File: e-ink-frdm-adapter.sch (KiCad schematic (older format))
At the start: 23 parts, among them P1 TE-2-1734592-4, P2 68000-110HLF, Q1 MF-DSC-SOT233-BSS138

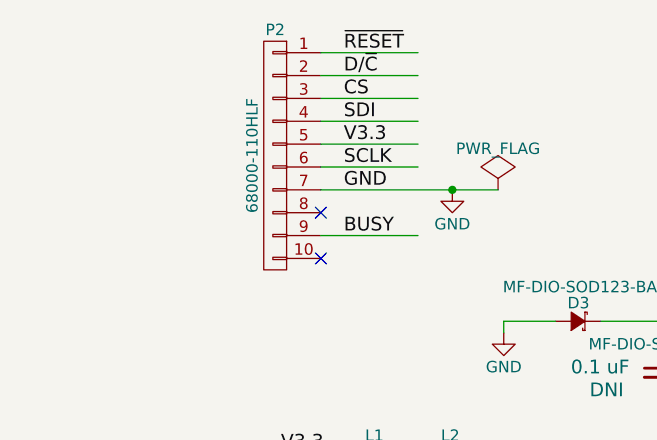
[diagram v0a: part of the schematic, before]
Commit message: Use house part for pin header
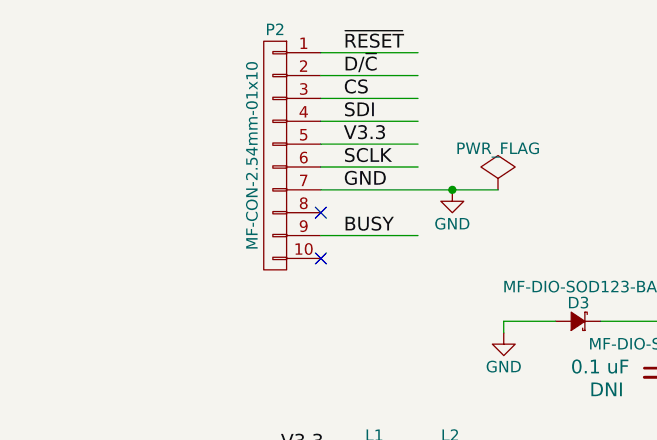
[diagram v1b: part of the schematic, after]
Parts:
- P2: value 68000-110HLF -> MF-CON-2.54mm-01x10
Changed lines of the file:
@@
 P 3275 2825
 F 0 "P2" H 3275 3375 50  0000 C CNN
-F 1 "68000-110HLF" V 3375 2825 50  0000 C CNN
+F 1 "MF-CON-2.54mm-01x10" V 3375 2825 50  0000 C CNN
 F 2 "Pin_Headers:Pin_Header_Straight_1x10" H 3275 2825 50  0001 C CNN
 F 3 "" H 3275 2825 50  0000 C CNN
